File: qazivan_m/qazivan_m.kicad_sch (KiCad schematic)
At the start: 97 parts, among them J1 AVR-ISP-6, J3 Conn_01x04_Female, U1 ATmega32U4-AU, Y1 16MHz

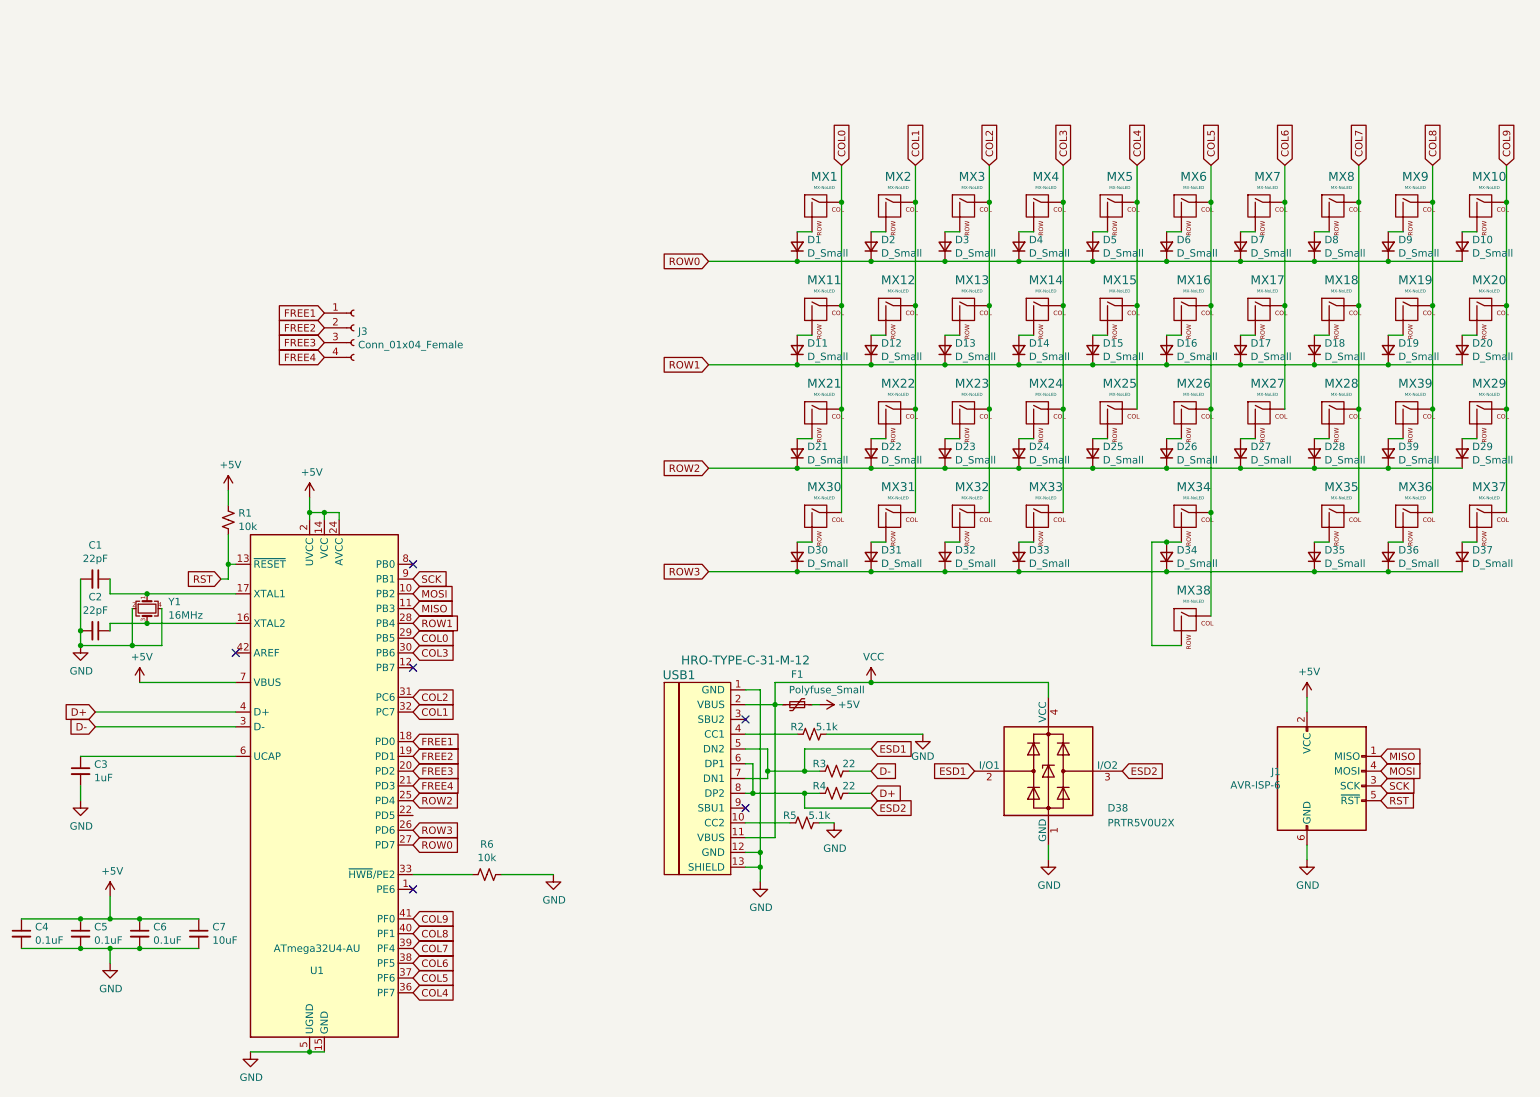
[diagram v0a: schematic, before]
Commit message: fixed bottom row, adding gamer row
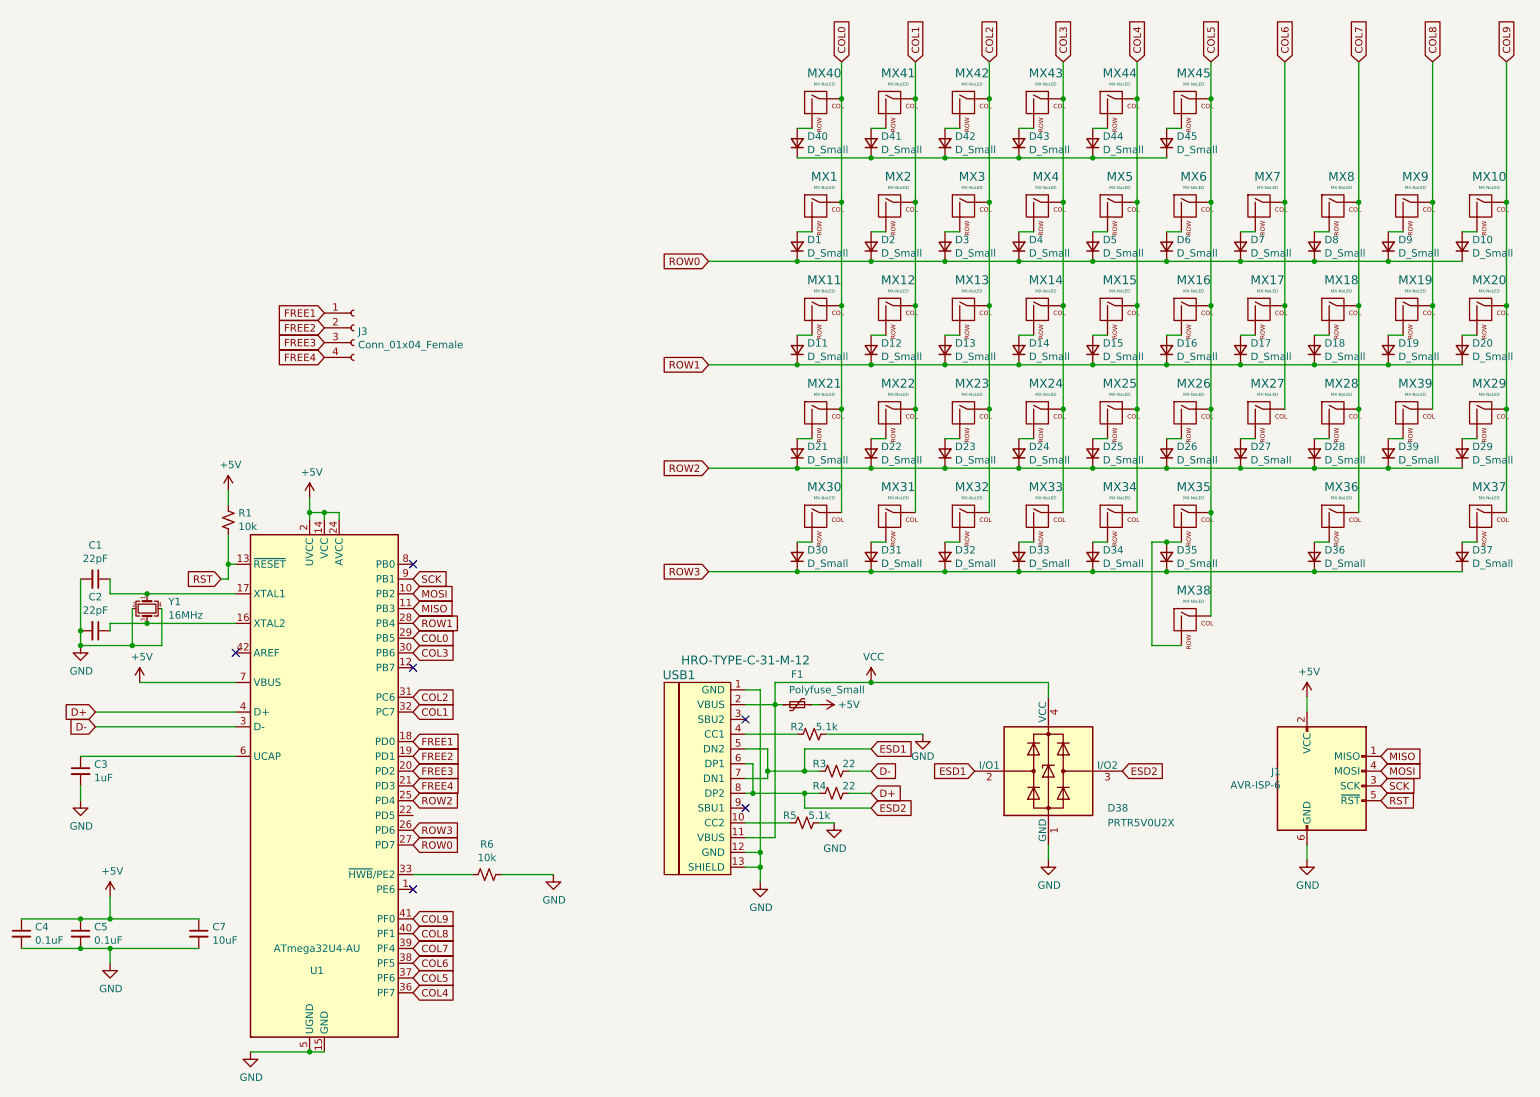
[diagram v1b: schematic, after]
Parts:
- removed C6: 0.1uF, Capacitor_SMD:C_0805_2012Metric, symbol Device:C_Small
- added D40, D41, D42, D43, D44, D45: D_Small, Diode_SMD:D_SOD-123, symbol Device:D_Small
- added MX40, MX41, MX42, MX43, MX44, MX45: MX-NoLED, MX_Only:MXOnly-1U-Hotswap, symbol MX_Alps_Hybrid:MX-NoLED
- MX33: footprint MX_Only:MXOnly-2.25U-Hotswap-ReversedStabilizers -> MX_Only:MXOnly-1U-Hotswap
- MX34: footprint MX_Only:MXOnly-2U-Hotswap-ReversedStabilizers -> MX_Only:MXOnly-2.25U-Hotswap-ReversedStabilizers
- MX35: footprint MX_Only:MXOnly-1U-Hotswap -> MX_Only:MXOnly-2U-Hotswap-ReversedStabilizers
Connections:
- net COL0: now also MX40.1 (COL)
- net COL1: now also MX41.1 (COL)
- net COL2: now also MX42.1 (COL)
- net COL3: now also MX43.1 (COL)
- net COL4: now also MX34.1 (COL), MX44.1 (COL)
- net COL5: now also MX35.1 (COL), MX45.1 (COL); no longer MX34.1 (COL)
- net COL7: now also MX36.1 (COL); no longer MX35.1 (COL)
- net COL8: no longer MX36.1 (COL)
- net at D34.2 (A), MX34.2 (ROW): no longer MX38.2 (ROW)
- net at D35.2 (A), MX35.2 (ROW): now also MX38.2 (ROW)
- new net: D44.2 (A), MX44.2 (ROW)
- new net: D40.1 (K), D41.1 (K), D42.1 (K), D43.1 (K), D44.1 (K), D45.1 (K)
- new net: D41.2 (A), MX41.2 (ROW)
- new net: D40.2 (A), MX40.2 (ROW)
- new net: D43.2 (A), MX43.2 (ROW)
- new net: D42.2 (A), MX42.2 (ROW)
- new net: D45.2 (A), MX45.2 (ROW)
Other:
- moved on the sheet: D34, D35, D36, MX34, MX35, MX36
